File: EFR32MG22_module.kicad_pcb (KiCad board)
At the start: 4 copper layers, 35.8 x 45.2 mm, 46 parts, among them J1 USB_C_Receptacle_PowerOnly_6P, J2 Conn_01x10, J3 ARM_2x5, J4 Conn_01x10, U1 EFR32MG22C224F512GN32, U2 TLV75533PDBV, U3 BME280, Y1 Crystal ECS-384-CDX-1983-TR3

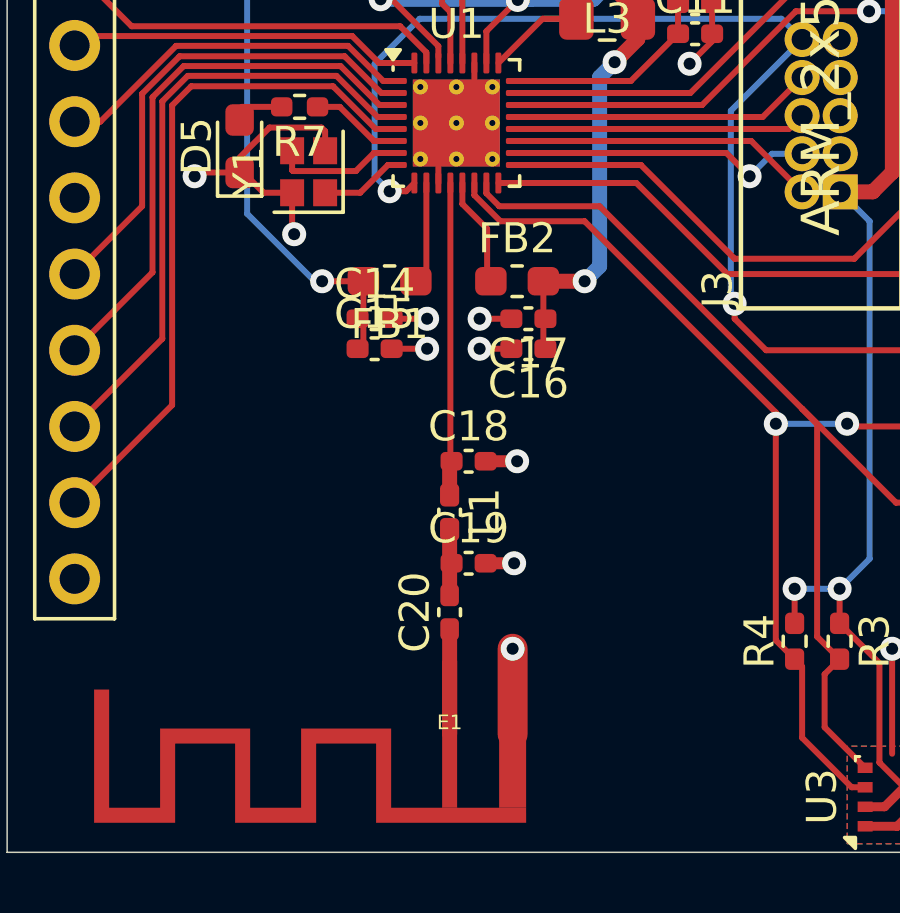
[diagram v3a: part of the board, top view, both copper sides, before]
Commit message: add impedance-controlled trace for antenna
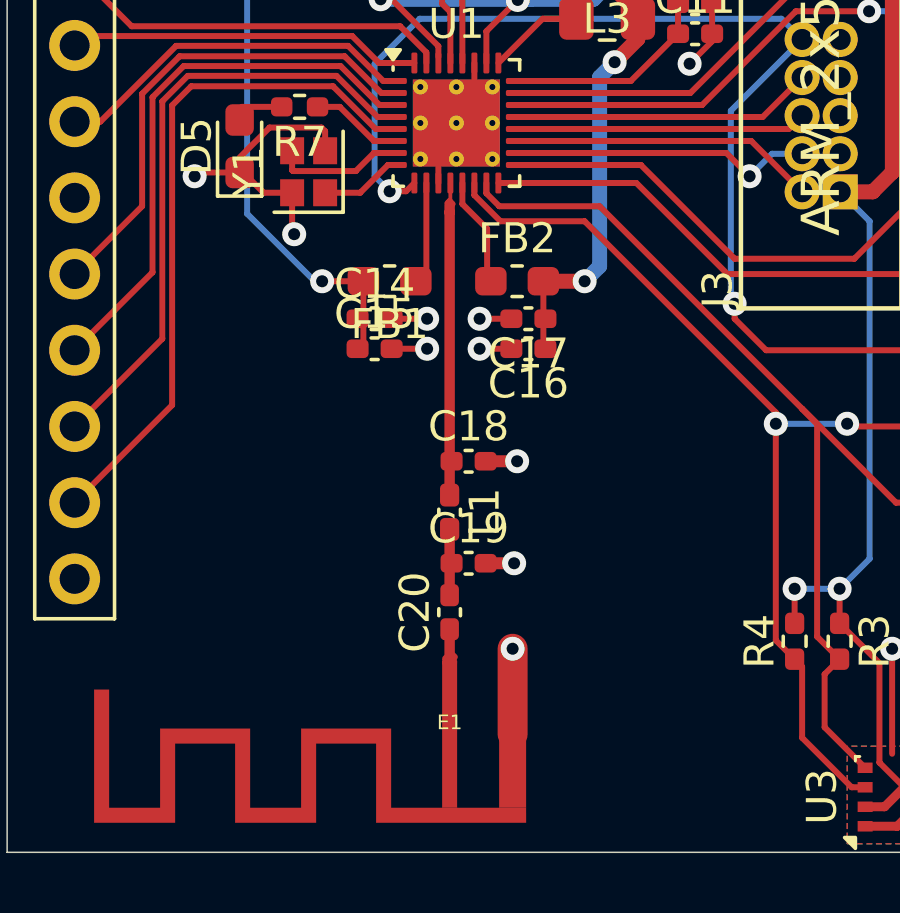
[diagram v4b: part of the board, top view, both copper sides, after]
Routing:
- net /RF2G4_IO: track 10.1 -> 10.7 mm
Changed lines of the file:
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@@
 		)
+	)
+	(gr_line
+		(start 144.5 124.425)
+		(end 144.35 124.575)
+		(stroke
+			(width 0.2)
+			(type default)
+		)
+		(layer "F.Cu")
+		(net 7)
+	)
+	(gr_circle
+		(center 144.5 124.7)
+		(end 144.5 124.55)
+		(stroke
+			(width 0.2)
+			(type default)
+		)
+		(fill none)
+		(layer "F.Cu")
+		(net 7)
+	)
+	(gr_line
+		(start 144.5 109.325)
+		(end 144.425 109.4)
+		(stroke
+			(width 0.2)
+			(type default)
+		)
+		(layer "F.Cu")
+		(net 5)
+	)
+	(gr_line
+		(start 144.675 124.525)
+		(end 144.575 124.425)
+		(stroke
+			(width 0.2)
+			(type default)
+		)
+		(layer "F.Cu")
+		(net 7)
+	)
+	(gr_line
+		(start 144.6 109.425)
+		(end 144.5 109.325)
+		(stroke
+			(width 0.2)
+			(type default)
+		)
+		(layer "F.Cu")
+		(net 5)
 	)
 	(gr_rect
@@
 	)
 	(segment
+		(start 144.5 109.7)
+		(end 144.5 109.475)
+		(width 0.34925)
+		(layer "F.Cu")
+		(net 5)
+	)
+	(segment
+		(start 144.5 108.75)
+		(end 144.525 108.725)
+		(width 0.127)
+		(layer "F.Cu")
+		(net 5)
+	)
+	(segment
+		(start 144.525 109.675)
+		(end 144.5 109.7)
+		(width 0.127)
+		(layer "F.Cu")
+		(net 5)
+	)
+	(segment
 		(start 144.525 108.725)
-		(end 144.525 117.7925)
-		(width 0.2)
+		(end 144.525 109.675)
+		(width 0.127)
 		(layer "F.Cu")
 		(net 5)
@@
 	(segment
 		(start 144.5 119.1275)
-		(end 144.5 118.065)
-		(width 0.5)
+		(end 144.5 109.7)
+		(width 0.34925)
 		(layer "F.Cu")
 		(net 5)
@@
 	(segment
 		(start 144.5 122.465)
-		(end 144.5 120.1725)
-		(width 0.5)
+		(end 144.5 120.2725)
+		(width 0.34925)
 		(layer "F.Cu")
 		(net 6)
@@
 		(start 144.5 127.1)
 		(end 144.5 123.6)
-		(width 0.5)
+		(width 0.34925)
 		(layer "F.Cu")
 		(net 7)

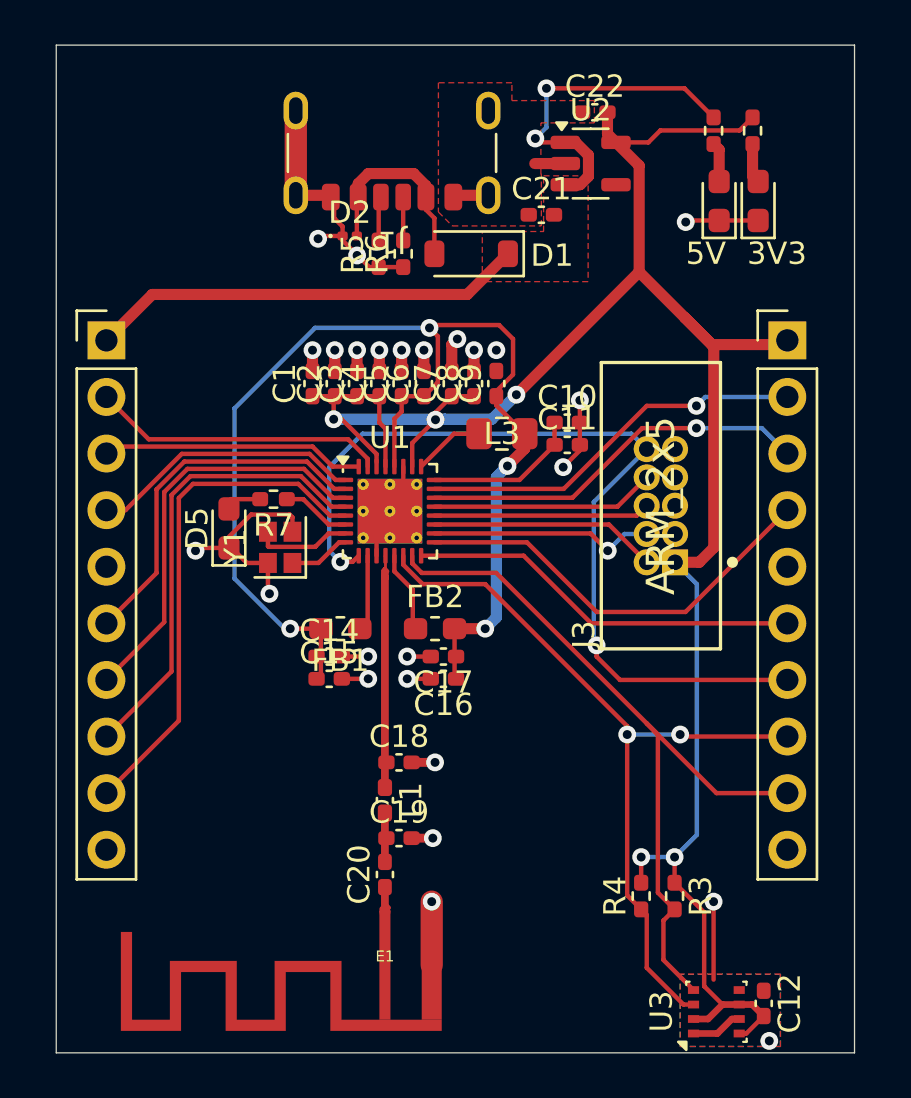
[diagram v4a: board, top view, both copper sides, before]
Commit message: minor tweaks for component selection
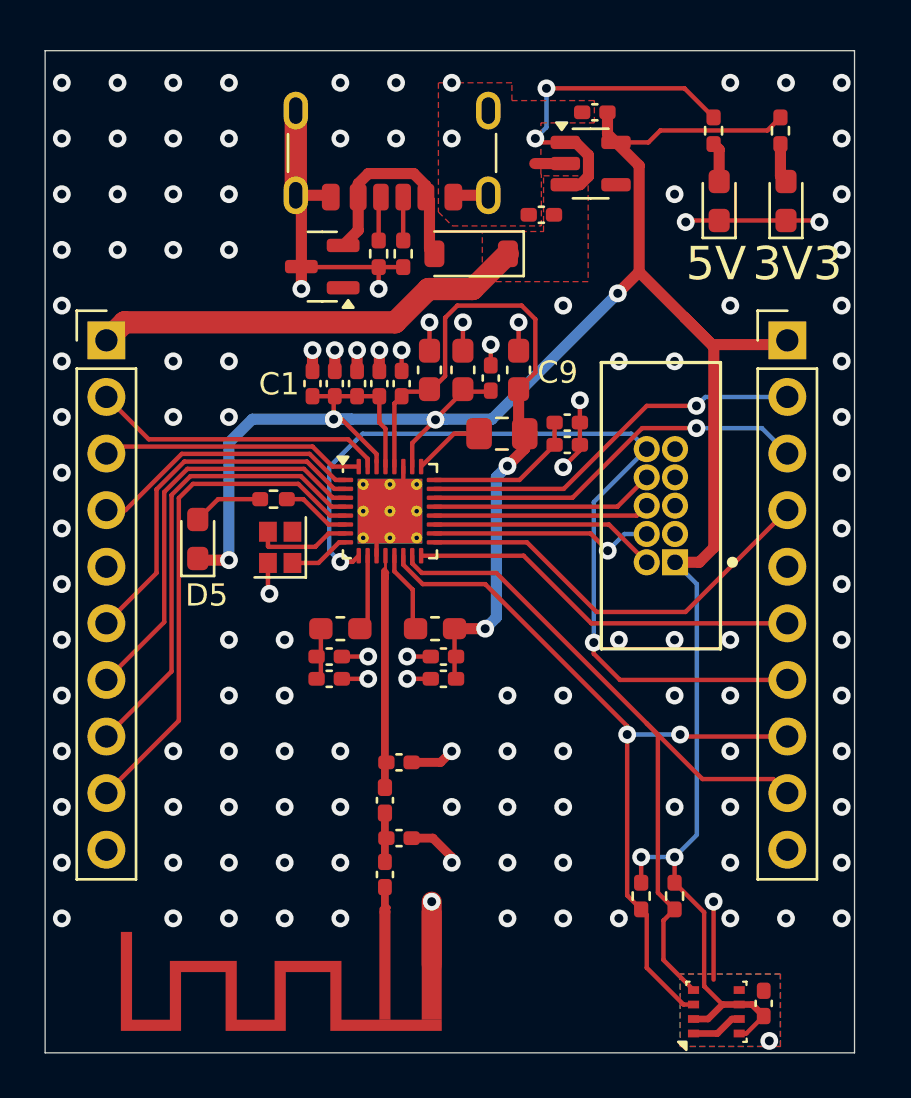
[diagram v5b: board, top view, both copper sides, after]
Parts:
- C10: value 1.0uF -> 1uF
- C17: value 100nF -> 0.1uF
- C6, C7, C9: footprint Capacitor_SMD:C_0402_1005Metric_Pad0.74x0.62mm_HandSolder -> Capacitor_SMD:C_0603_1608Metric_Pad1.08x0.95mm_HandSolder
- D2: value D_TVS -> SP0502BAHT; footprint Diode_SMD:D_0201_0603Metric -> Package_TO_SOT_SMD:SOT-23
- FB1, FB2: value 1-5.2uH 0.5-1 Ω -> BLM18AG102SN1
- R1, R2, R7: value 4.7k -> 82
- R3, R4: value 4.7k -> 5.1k
- moved D2 1.85 mm to (141.7, 95.8), turned to 180 degrees
- moved D5 1.48 mm to (136.1, 108.0)
- moved D4 1.25 mm to (162.5, 92.8)
- moved R2 1.25 mm to (162.2, 89.7)
- moved C9 1.17 mm to (150.5, 100.4)
- moved C7 0.79 mm to (148.0, 100.4)
- moved C8 0.79 mm to (149.2, 100.8)
- moved C6 0.66 mm to (146.5, 100.4)
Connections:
- D2 pad 1: GND -> unconnected-(D2-K-Pad1)
- D5 pad 1: GND -> +3.3V
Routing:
- net /DVDD: track 54.6 -> 32.9 mm, vias 4 -> 2
- net +3.3V: track 96.5 -> 110.5 mm, vias 5 -> 6
- net GND: track 56.1 -> 58.6 mm, vias 25 -> 129
- net Net-(D5-A): track 1.34 -> 3.18 mm
- net Net-(D1-A): track 8.95 -> 9.72 mm
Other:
- board size 35.8 x 45.2 mm -> 36.3 x 45 mm

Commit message: fix DRC
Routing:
- net /DVDD: track 32.9 -> 59.7 mm, vias 2 -> 4
- net GND: track 58.6 -> 63.0 mm, vias 129 -> 128
- net +3.3V: track 110.5 -> 109.7 mm
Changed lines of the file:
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@@
 		(pad "1" thru_hole rect
 			(at -2.54 0.635 90)
-			(size 1.17 1.17)
+			(size 1.1 1.1)
 			(drill 0.7)
 			(layers "*.Cu" "*.Mask")
@@
 		(pad "2" thru_hole circle
 			(at -2.54 -0.635 90)
-			(size 1.17 1.17)
+			(size 1.1 1.1)
 			(drill 0.7)
 			(layers "*.Cu" "*.Mask")
@@
 		(pad "3" thru_hole circle
 			(at -1.27 0.635 90)
-			(size 1.17 1.17)
+			(size 1.1 1.1)
 			(drill 0.7)
 			(layers "*.Cu" "*.Mask")
@@
 		(pad "4" thru_hole circle
 			(at -1.27 -0.635 90)
-			(size 1.17 1.17)
+			(size 1.1 1.1)
 			(drill 0.7)
 			(layers "*.Cu" "*.Mask")
@@
 		(pad "5" thru_hole circle
 			(at 0 0.635 90)
-			(size 1.17 1.17)
+			(size 1.1 1.1)
 			(drill 0.7)
 			(layers "*.Cu" "*.Mask")
@@
 		(pad "6" thru_hole circle
 			(at 0 -0.635 90)
-			(size 1.17 1.17)
+			(size 1.1 1.1)
 			(drill 0.7)
 			(layers "*.Cu" "*.Mask")
@@
 		(pad "7" thru_hole circle
 			(at 1.27 0.635 90)
-			(size 1.17 1.17)
+			(size 1.1 1.1)
 			(drill 0.7)
 			(layers "*.Cu" "*.Mask")
@@
 		(pad "8" thru_hole circle
 			(at 1.27 -0.635 90)
-			(size 1.17 1.17)
+			(size 1.1 1.1)
 			(drill 0.7)
 			(layers "*.Cu" "*.Mask")
@@
 		(pad "9" thru_hole circle
 			(at 2.54 0.635 90)
-			(size 1.17 1.17)
+			(size 1.1 1.1)
 			(drill 0.7)
 			(layers "*.Cu" "*.Mask")
@@
 		(pad "10" thru_hole circle
 			(at 2.54 -0.635 90)
-			(size 1.17 1.17)
+			(size 1.1 1.1)
 			(drill 0.7)
 			(layers "*.Cu" "*.Mask")
@@
 	)
 	(segment
-		(start 140.7725 95.7725)
-		(end 140.75 95.75)
-		(width 0.2)
-		(layer "F.Cu")
-		(net 1)
-	)
-	(segment
 		(start 140.5 92.55)
 		(end 141.99 92.55)
@@
 	)
 	(segment
+		(start 139.774 106.87)
+		(end 138.726 106.87)
+		(width 0.2)
+		(layer "F.Cu")
+		(net 1)
+	)
+	(segment
+		(start 148 99.525)
+		(end 148.975 99.525)
+		(width 0.2)
+		(layer "F.Cu")
+		(net 1)
+	)
+	(segment
 		(start 146.65 121.4)
 		(end 147.5 122.25)
@@
 	)
 	(segment
+		(start 140.35 107.446)
+		(end 139.774 106.87)
+		(width 0.2)
+		(layer "F.Cu")
+		(net 1)
+	)
+	(segment
 		(start 146.6 127.1)
 		(end 146.6 124.25)
@@
 	)
 	(segment
+		(start 138.52 108.32)
+		(end 139.25 109.05)
+		(width 0.2)
+		(layer "F.Cu")
+		(net 1)
+	)
+	(segment
 		(start 145.325 104.725)
 		(end 145.325 106.125)
@@
 	)
 	(segment
+		(start 148.975 99.525)
+		(end 149.25 99.25)
+		(width 0.2)
+		(layer "F.Cu")
+		(net 1)
+	)
+	(segment
 		(start 144.125 108.725)
 		(end 144.125 107.325)
@@
 	)
 	(segment
+		(start 138.726 106.87)
+		(end 138.52 107.076)
+		(width 0.2)
+		(layer "F.Cu")
+		(net 1)
+	)
+	(segment
 		(start 142.5675 114.25)
 		(end 143.75 114.25)
@@
 	)
 	(segment
-		(start 148 99.6375)
-		(end 148 98.25)
-		(width 0.2)
-		(layer "F.Cu")
-		(net 1)
-	)
-	(segment
 		(start 140.75 95.75)
 		(end 140.75 92.8)
@@
 	)
 	(segment
+		(start 138.52 107.076)
+		(end 138.52 108.32)
+		(width 0.2)
+		(layer "F.Cu")
+		(net 1)
+	)
+	(segment
 		(start 144.22 96.75)
 		(end 144.22 95.7725)
@@
 	)
 	(via
-		(at 148 98.25)
-		(size 0.8)
-		(drill 0.4)
-		(layers "F.Cu" "B.Cu")
-		(net 1)
-	)
-	(via
 		(at 160 112.5)
 		(size 0.8)
@@
 	)
 	(segment
-		(start 143 102.6)
-		(end 142.2 102.6)
+		(start 142.2 102.6)
+		(end 147.2 102.6)
 		(width 0.5)
 		(layer "B.Cu")
@@
 	(segment
 		(start 138.55 102.6)
-		(end 143 102.6)
-		(width 0.5)
-		(layer "B.Cu")
-		(net 2)
-	)
-	(segment
-		(start 147.2 102.6)
-		(end 143 102.6)
+		(end 142.2 102.6)
 		(width 0.5)
 		(layer "B.Cu")
@@
 	)
 	(segment
+		(start 147.627 97.623)
+		(end 150.759712 97.623)
+		(width 0.2)
+		(layer "F.Cu")
+		(net 3)
+	)
+	(segment
 		(start 144.925 101.8925)
 		(end 145.25 101.5675)
@@
 	)
 	(segment
-		(start 147.202 98.048)
-		(end 147.75 97.5)
+		(start 147.202 100.6605)
+		(end 147.202 98.048)
 		(width 0.2)
 		(layer "F.Cu")
@@
 	)
 	(segment
-		(start 150.636712 97.5)
-		(end 151.25 98.113288)
+		(start 147.202 98.048)
+		(end 147.627 97.623)
 		(width 0.2)
 		(layer "F.Cu")
@@
 	)
 	(segment
-		(start 146.5 101.3625)
-		(end 145.455 101.3625)
+		(start 141.625 112)
+		(end 141.025 111.4)
 		(width 0.2)
 		(layer "F.Cu")
@@
 	)
 	(segment
-		(start 147.75 97.5)
-		(end 150.636712 97.5)
+		(start 151.25 100.5)
+		(end 150.5 101.25)
 		(width 0.2)
 		(layer "F.Cu")
@@
 	)
 	(segment
-		(start 150.775 103.923)
-		(end 150 104.698)
-		(width 0.5)
+		(start 145.455 101.3625)
+		(end 146.5 101.3625)
+		(width 0.2)
 		(layer "F.Cu")
 		(net 3)
 	)
 	(segment
-		(start 150.5 102.975)
-		(end 150.5 101.25)
-		(width 0.5)
+		(start 151.25 98.113288)
+		(end 151.25 100.5)
+		(width 0.2)
 		(layer "F.Cu")
 		(net 3)
 	)
 	(segment
-		(start 147.625 112)
-		(end 147.625 114.1825)
+		(start 150.759712 97.623)
+		(end 151.25 98.113288)
 		(width 0.2)
 		(layer "F.Cu")
@@
 	)
 	(segment
-		(start 151.25 98.113288)
-		(end 151.25 100.5)
+		(start 141.025 111.4)
+		(end 136.64 111.4)
 		(width 0.2)
 		(layer "F.Cu")
@@
 	)
 	(segment
-		(start 150.775 103.25)
-		(end 150.775 103.923)
+		(start 150.775 103.923)
+		(end 150 104.698)
 		(width 0.5)
 		(layer "F.Cu")
@@
 	)
 	(segment
-		(start 147.202 100.6605)
-		(end 147.202 98.048)
+		(start 150.5 102.975)
+		(end 150.5 101.25)
+		(width 0.5)
+		(layer "F.Cu")
+		(net 3)
+	)
+	(segment
+		(start 147.625 112)
+		(end 147.625 114.1825)
 		(width 0.2)
 		(layer "F.Cu")
@@
 	)
 	(segment
+		(start 150.775 103.25)
+		(end 150.775 103.923)
+		(width 0.5)
+		(layer "F.Cu")
+		(net 3)
+	)
+	(segment
 		(start 149 112)
 		(end 147.625 112)
@@
 		(net 3)
 	)
-	(segment
-		(start 151.25 100.5)
-		(end 150.5 101.25)
-		(width 0.2)
-		(layer "F.Cu")
+	(via
+		(at 136.64 111.4)
+		(size 0.8)
+		(drill 0.4)
+		(layers "F.Cu" "B.Cu")
 		(net 3)
 	)
@@
 	)
 	(via
+		(at 147.301358 97.784)
+		(size 0.8)
+		(drill 0.4)
+		(layers "F.Cu" "B.Cu")
+		(net 3)
+	)
+	(via
 		(at 149 112)
 		(size 0.8)
@@
 	)
 	(segment
+		(start 147.140358 97.623)
+		(end 141.490288 97.623)
+		(width 0.2)
+		(layer "B.Cu")
+		(net 3)
+	)
+	(segment
+		(start 147.301358 97.784)
+		(end 147.140358 97.623)
+		(width 0.2)
+		(layer "B.Cu")
+		(net 3)
+	)
+	(segment
 		(start 149.5 111.5)
 		(end 149 112)
@@
 		(layer "B.Cu")
 		(net 3)
+	)
+	(segment
+		(start 136.64 102.473288)
+		(end 136.64 111.4)
+		(width 0.2)
+		(layer "B.Cu")
+		(net 3)
+	)
+	(segment
+		(start 141.490288 97.623)
+		(end 136.64 102.473288)
+		(width 0.2)
+		(layer "B.Cu")
+		(net 3)

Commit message: silkscreen
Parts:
- R1: value 82 -> 220
- moved C11 1.55 mm to (151.5, 104.8)
- moved C16 1.00 mm to (147.1, 113.2)
- moved C17 1.00 mm to (147.1, 114.2)
- moved C10 0.50 mm to (152.2, 103.0), turned to 90 degrees
- turned D5 to -90 degrees
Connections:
- D5 pad 1: +3.3V -> Net-(D5-K)
- D5 pad 2: Net-(D5-A) -> +3.3V
- R7 pad 2: Net-(D5-A) -> Net-(D5-K)
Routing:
- net Net-(D5-K): track 0.00 -> 3.18 mm
- net Net-(D5-A): track 3.18 -> 0.00 mm
- net /RESET_N: track 39.9 -> 41.0 mm
- net Net-(U1-DECOUPLE): track 7.04 -> 6.04 mm
- net GND: track 63.0 -> 62.0 mm, vias 128 -> 127
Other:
- board text added: "A00"
- board text added: "A05"
- board text added: "A06"
- board text added: "B00"
- board text added: "C00"
- board text added: "C01"
- board text added: "C02"
- board text added: "C03"
- board text added: "C04"
- board text added: "D00"
- board text added: "D01"
- board text added: "G"
- board text added: "GND"
- board text added: "J1"
- board text added: "J3"
- board text added: "RESET"
- board text added: "SCL"
- board text added: "SDA"
- board text added: "VBUS"
- board text added: "⏄"
